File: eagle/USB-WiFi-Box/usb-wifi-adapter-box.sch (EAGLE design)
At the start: 12 parts

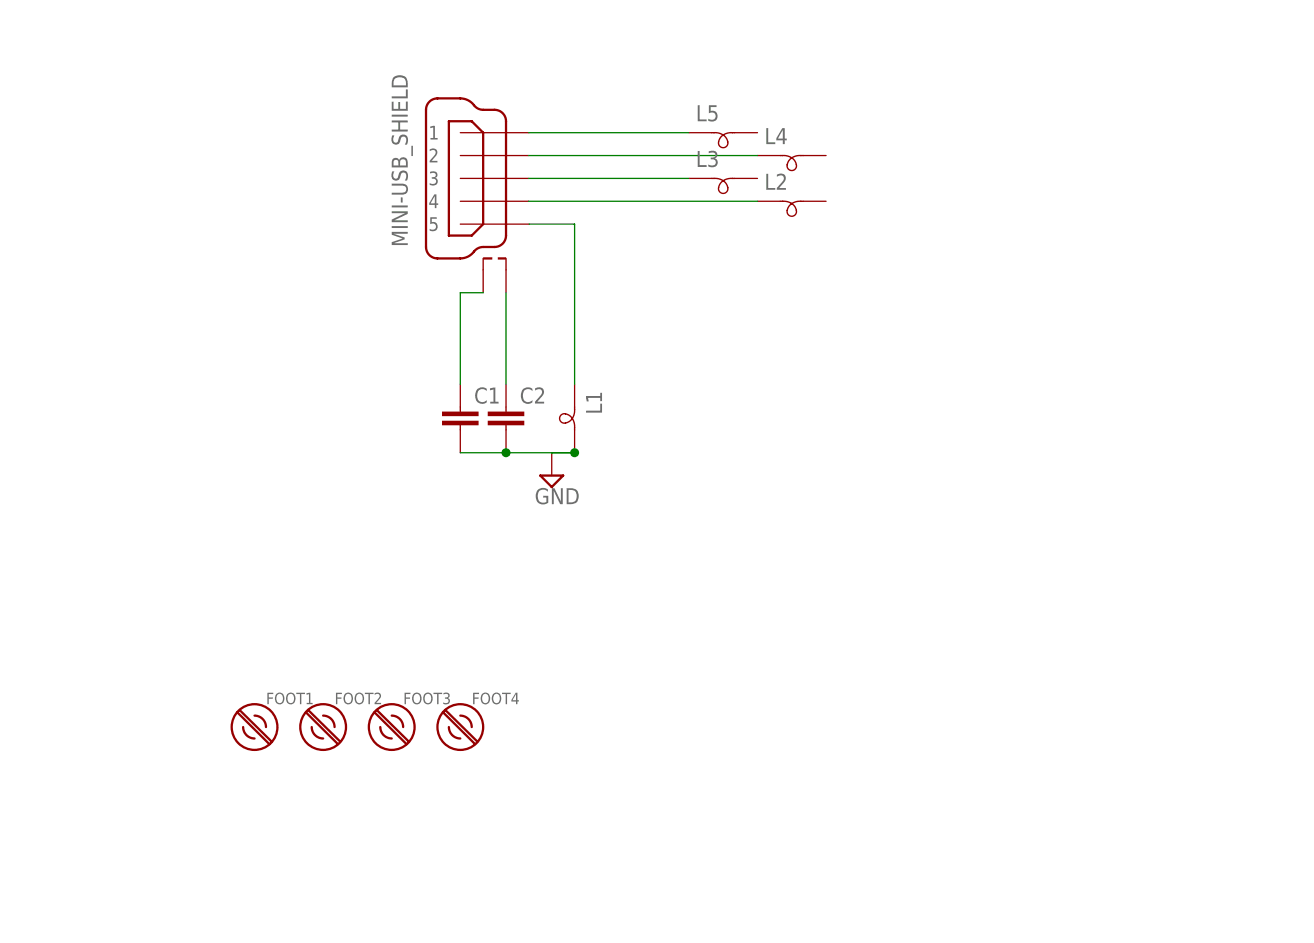
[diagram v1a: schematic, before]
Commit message: Measured USB board, finished schematic
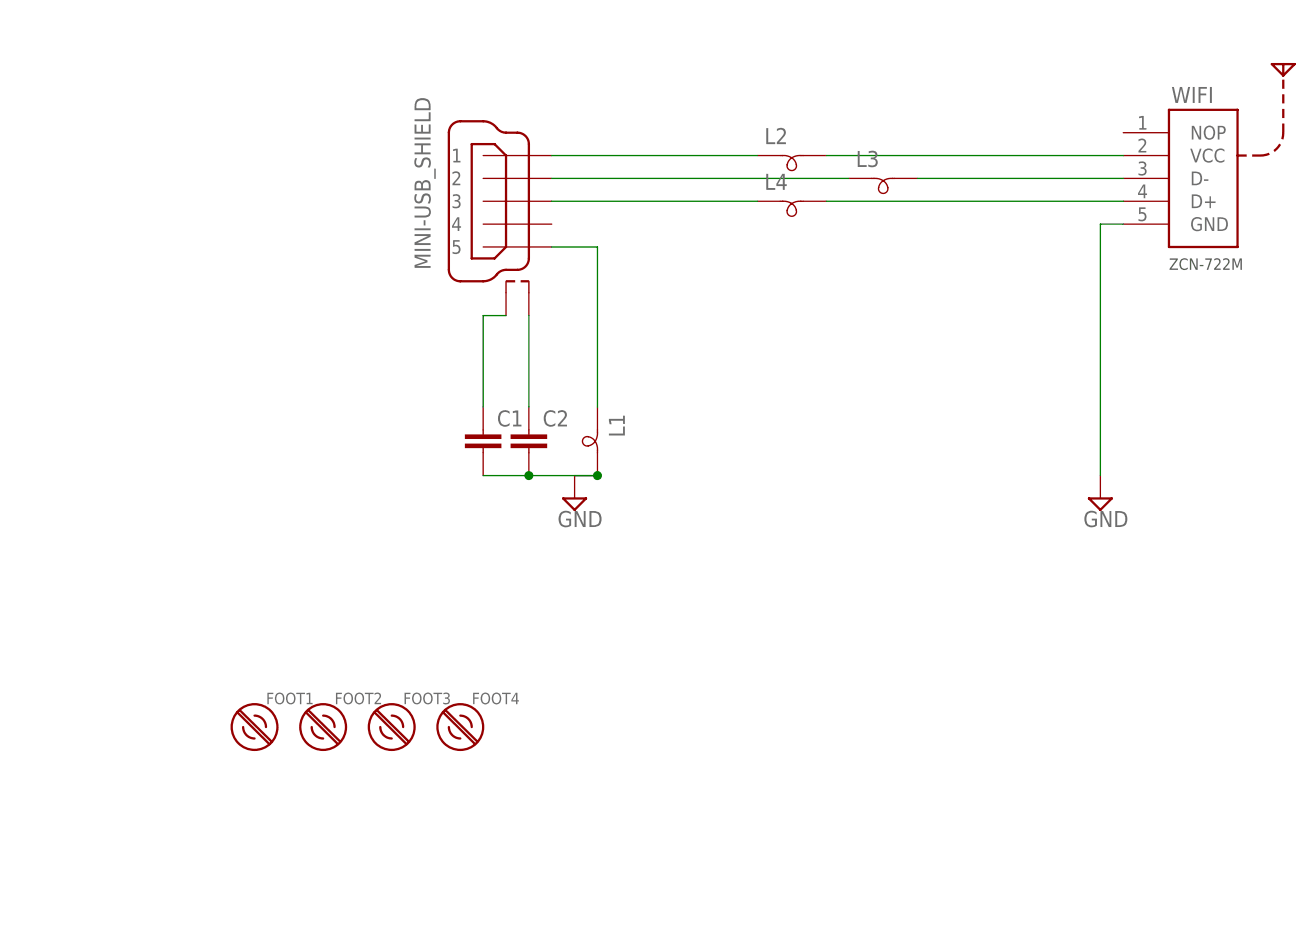
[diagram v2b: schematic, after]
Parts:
- removed L5: (no value), dxwifi:INDUCTOR-BEAD
- added WIFI: ZCN-722M, dxwifi:ZCN-722M
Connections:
- removed net N$2: CONN1G41.4, L2.1
- new net N$10: L4.2, WIFI.D+
- new net N$8: L2.2, WIFI.VCC
- new net N$9: L3.2, WIFI.D-
- net GND: now also WIFI.GND
- net N$3: now also L4.1; no longer L3.1
- net N$4: now also L3.1; no longer L4.1
- net N$5: now also L2.1; no longer L5.1
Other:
- moved on the sheet: C1, C2, L1, L2, L3, L4
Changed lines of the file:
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@@
 <part name="CONN1" library="dxwifi" deviceset="MINI-USB_SHIELD" device=""/>
 <part name="L1" library="dxwifi" deviceset="INDUCTOR-BEAD" device=""/>
+<part name="L4" library="dxwifi" deviceset="INDUCTOR-BEAD" device=""/>
+<part name="L3" library="dxwifi" deviceset="INDUCTOR-BEAD" device=""/>
 <part name="L2" library="dxwifi" deviceset="INDUCTOR-BEAD" device=""/>
-<part name="L3" library="dxwifi" deviceset="INDUCTOR-BEAD" device=""/>
-<part name="L4" library="dxwifi" deviceset="INDUCTOR-BEAD" device=""/>
-<part name="L5" library="dxwifi" deviceset="INDUCTOR-BEAD" device=""/>
 <part name="C1" library="rcl" deviceset="C-EU" device="C0805"/>
 <part name="C2" library="rcl" deviceset="C-EU" device="C0805"/>
@@
 <part name="FOOT4" library="mount-2" deviceset="_4-BARE_MOUNTING_HOLE" device="/.400"/>
 <part name="FRAME1" library="frames" deviceset="A5L-LOC" device=""/>
+<part name="WIFI" library="dxwifi" deviceset="ZCN-722M" device=""/>
+<part name="SUPPLY2" library="supply2" deviceset="GND" device=""/>
 </parts>
 <sheets>
@@
 </plain>
 <instances>
-<instance part="CONN1" gate="G41" x="50.8" y="91.44" smashed="yes" rot="MR0">
-<attribute name="VALUE" x="40.64" y="83.82" size="1.778" layer="96" font="vector" rot="MR90"/>
+<instance part="CONN1" gate="G41" x="53.34" y="88.9" smashed="yes" rot="MR0">
+<attribute name="VALUE" x="43.18" y="81.28" size="1.778" layer="96" font="vector" rot="MR90"/>
 </instance>
-<instance part="L1" gate="G$1" x="60.96" y="63.5" rot="R270"/>
-<instance part="L2" gate="G$1" x="86.36" y="88.9"/>
-<instance part="L3" gate="G$1" x="78.74" y="91.44"/>
-<instance part="L4" gate="G$1" x="86.36" y="93.98"/>
-<instance part="L5" gate="G$1" x="78.74" y="96.52"/>
-<instance part="C1" gate="G$1" x="48.26" y="66.04"/>
-<instance part="C2" gate="G$1" x="53.34" y="66.04"/>
-<instance part="SUPPLY1" gate="GND" x="58.42" y="58.42"/>
-<instance part="CONN1" gate="S" x="53.34" y="81.28" smashed="yes"/>
+<instance part="L1" gate="G$1" x="63.5" y="60.96" rot="R270"/>
+<instance part="L4" gate="G$1" x="86.36" y="88.9"/>
+<instance part="L3" gate="G$1" x="96.52" y="91.44"/>
+<instance part="L2" gate="G$1" x="86.36" y="93.98"/>
+<instance part="C1" gate="G$1" x="50.8" y="63.5"/>
+<instance part="C2" gate="G$1" x="55.88" y="63.5"/>
+<instance part="SUPPLY1" gate="GND" x="60.96" y="55.88"/>
+<instance part="CONN1" gate="S" x="55.88" y="78.74" smashed="yes"/>
 <instance part="FOOT1" gate="MT" x="25.4" y="30.48" smashed="yes">
 <attribute name="NAME" x="26.67" y="33.02" size="1.27" layer="95"/>
@@
 </instance>
 <instance part="FRAME1" gate="G$1" x="0" y="0"/>
+<instance part="WIFI" gate="G$1" x="129.54" y="91.44" smashed="yes">
+<attribute name="NAME" x="127.254" y="99.822" size="1.778" layer="95" font="vector"/>
+</instance>
+<instance part="SUPPLY2" gate="GND" x="119.38" y="55.88"/>
 </instances>
 <busses>
 </busses>
 <nets>
-<net name="N$2" class="0">
-<segment>
-<pinref part="L2" gate="G$1" pin="1"/>
-<pinref part="CONN1" gate="G41" pin="4"/>
-<wire x1="55.88" y1="88.9" x2="81.28" y2="88.9" width="0.1524" layer="91"/>
-</segment>
-</net>
 <net name="N$3" class="0">
 <segment>
 <pinref part="CONN1" gate="G41" pin="3"/>
-<pinref part="L3" gate="G$1" pin="1"/>
-<wire x1="55.88" y1="91.44" x2="73.66" y2="91.44" width="0.1524" layer="91"/>
+<pinref part="L4" gate="G$1" pin="1"/>
+<wire x1="58.42" y1="88.9" x2="81.28" y2="88.9" width="0.1524" layer="91"/>
 </segment>
 </net>
@@
 <segment>
 <pinref part="CONN1" gate="G41" pin="2"/>
-<pinref part="L4" gate="G$1" pin="1"/>
-<wire x1="55.88" y1="93.98" x2="81.28" y2="93.98" width="0.1524" layer="91"/>
+<pinref part="L3" gate="G$1" pin="1"/>
+<wire x1="58.42" y1="91.44" x2="91.44" y2="91.44" width="0.1524" layer="91"/>
 </segment>
 </net>
@@
 <segment>
 <pinref part="CONN1" gate="G41" pin="1"/>
-<pinref part="L5" gate="G$1" pin="1"/>
-<wire x1="55.88" y1="96.52" x2="73.66" y2="96.52" width="0.1524" layer="91"/>
+<pinref part="L2" gate="G$1" pin="1"/>
+<wire x1="58.42" y1="93.98" x2="81.28" y2="93.98" width="0.1524" layer="91"/>
 </segment>
 </net>
@@
 <pinref part="C1" gate="G$1" pin="2"/>
 <pinref part="C2" gate="G$1" pin="2"/>
-<wire x1="48.26" y1="60.96" x2="53.34" y2="60.96" width="0.1524" layer="91"/>
+<wire x1="50.8" y1="58.42" x2="55.88" y2="58.42" width="0.1524" layer="91"/>
 <pinref part="L1" gate="G$1" pin="2"/>
-<wire x1="53.34" y1="60.96" x2="60.96" y2="60.96" width="0.1524" layer="91"/>
-<junction x="53.34" y="60.96"/>
+<wire x1="55.88" y1="58.42" x2="63.5" y2="58.42" width="0.1524" layer="91"/>
+<junction x="55.88" y="58.42"/>
 <pinref part="SUPPLY1" gate="GND" pin="GND"/>
-<junction x="60.96" y="60.96"/>
-<wire x1="60.96" y1="60.96" x2="58.42" y2="60.96" width="0.1524" layer="91"/>
+<junction x="63.5" y="58.42"/>
+<wire x1="63.5" y1="58.42" x2="60.96" y2="58.42" width="0.1524" layer="91"/>
+</segment>
+<segment>
+<pinref part="WIFI" gate="G$1" pin="GND"/>
+<pinref part="SUPPLY2" gate="GND" pin="GND"/>
+<wire x1="121.92" y1="86.36" x2="119.38" y2="86.36" width="0.1524" layer="91"/>
+<wire x1="119.38" y1="86.36" x2="119.38" y2="58.42" width="0.1524" layer="91"/>
 </segment>
 </net>
@@
 <pinref part="CONN1" gate="G41" pin="5"/>
 <pinref part="L1" gate="G$1" pin="1"/>
-<wire x1="55.88" y1="86.36" x2="60.96" y2="86.36" width="0.1524" layer="91"/>
-<wire x1="60.96" y1="86.36" x2="60.96" y2="68.58" width="0.1524" layer="91"/>
+<wire x1="58.42" y1="83.82" x2="63.5" y2="83.82" width="0.1524" layer="91"/>
+<wire x1="63.5" y1="83.82" x2="63.5" y2="66.04" width="0.1524" layer="91"/>
 </segment>
 </net>
@@
 <pinref part="CONN1" gate="S" pin="S2"/>
 <pinref part="C2" gate="G$1" pin="1"/>
-<wire x1="53.34" y1="78.74" x2="53.34" y2="68.58" width="0.1524" layer="91"/>
+<wire x1="55.88" y1="76.2" x2="55.88" y2="66.04" width="0.1524" layer="91"/>
 </segment>
 </net>
@@
 <segment>
 <pinref part="CONN1" gate="S" pin="S1"/>
-<wire x1="50.8" y1="78.74" x2="48.26" y2="78.74" width="0.1524" layer="91"/>
+<wire x1="53.34" y1="76.2" x2="50.8" y2="76.2" width="0.1524" layer="91"/>
 <pinref part="C1" gate="G$1" pin="1"/>
-<wire x1="48.26" y1="78.74" x2="48.26" y2="68.58" width="0.1524" layer="91"/>
+<wire x1="50.8" y1="76.2" x2="50.8" y2="66.04" width="0.1524" layer="91"/>
 </segment>
 </net>
+<net name="N$8" class="0">
+<segment>
+<pinref part="L2" gate="G$1" pin="2"/>
+<pinref part="WIFI" gate="G$1" pin="VCC"/>
+<wire x1="88.9" y1="93.98" x2="121.92" y2="93.98" width="0.1524" layer="91"/>
+</segment>
+</net>
+<net name="N$9" class="0">
+<segment>
+<pinref part="L3" gate="G$1" pin="2"/>
+<pinref part="WIFI" gate="G$1" pin="D-"/>
+<wire x1="99.06" y1="91.44" x2="121.92" y2="91.44" width="0.1524" layer="91"/>
+</segment>
+</net>
+<net name="N$10" class="0">
+<segment>
+<pinref part="L4" gate="G$1" pin="2"/>
+<pinref part="WIFI" gate="G$1" pin="D+"/>
+<wire x1="88.9" y1="88.9" x2="121.92" y2="88.9" width="0.1524" layer="91"/>
+</segment>
+</net>

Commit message: board layout v1, using one wire for VCC, fixed slots in USB part
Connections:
- net N$1 renamed SHEILDGND1
- net N$10 renamed D+
- net N$3 renamed D+OUT
- net N$4 renamed D-OUT
- net N$5 renamed VCC_OUT
- net N$6 renamed GNDOUT
- net N$7 renamed SHIELDGND2
- net N$8 renamed VCC
- net N$9 renamed D-
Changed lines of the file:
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@@
 </busses>
 <nets>
-<net name="N$3" class="0">
+<net name="D+OUT" class="0">
 <segment>
 <pinref part="CONN1" gate="G41" pin="3"/>
@@
 </segment>
 </net>
-<net name="N$4" class="0">
+<net name="D-OUT" class="0">
 <segment>
 <pinref part="CONN1" gate="G41" pin="2"/>
@@
 </segment>
 </net>
-<net name="N$5" class="0">
+<net name="VCC_OUT" class="0">
 <segment>
 <pinref part="CONN1" gate="G41" pin="1"/>
@@
 </segment>
 </net>
-<net name="N$6" class="0">
+<net name="GNDOUT" class="0">
 <segment>
 <pinref part="CONN1" gate="G41" pin="5"/>
@@
 </segment>
 </net>
-<net name="N$1" class="0">
+<net name="SHEILDGND1" class="0">
 <segment>
 <pinref part="CONN1" gate="S" pin="S2"/>
@@
 </segment>
 </net>
-<net name="N$7" class="0">
+<net name="SHIELDGND2" class="0">
 <segment>
 <pinref part="CONN1" gate="S" pin="S1"/>
@@
 </segment>
 </net>
-<net name="N$8" class="0">
+<net name="VCC" class="0">
 <segment>
 <pinref part="L2" gate="G$1" pin="2"/>
@@
 </segment>
 </net>
-<net name="N$9" class="0">
+<net name="D-" class="0">
 <segment>
 <pinref part="L3" gate="G$1" pin="2"/>
@@
 </segment>
 </net>
-<net name="N$10" class="0">
+<net name="D+" class="0">
 <segment>
 <pinref part="L4" gate="G$1" pin="2"/>

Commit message: fix routing issues
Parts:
- added TP1: PTR1PAD1-13, testpad:PTR1PAD1-13
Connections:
- new net N$1: TP1.TP, WIFI.NOP
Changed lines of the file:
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@@
 <part name="WIFI" library="dxwifi" deviceset="ZCN-722M" device=""/>
 <part name="SUPPLY2" library="supply2" deviceset="GND" device=""/>
+<part name="TP1" library="testpad" deviceset="PTR1" device="PAD1-13"/>
 </parts>
 <sheets>
@@
 </instance>
 <instance part="SUPPLY2" gate="GND" x="119.38" y="55.88"/>
+<instance part="TP1" gate="G$1" x="119.38" y="99.06" rot="R180"/>
 </instances>
 <busses>
@@
 </segment>
 </net>
+<net name="N$1" class="0">
+<segment>
+<pinref part="TP1" gate="G$1" pin="TP"/>
+<pinref part="WIFI" gate="G$1" pin="NOP"/>
+<wire x1="119.38" y1="96.52" x2="121.92" y2="96.52" width="0.1524" layer="91"/>
+</segment>
+</net>

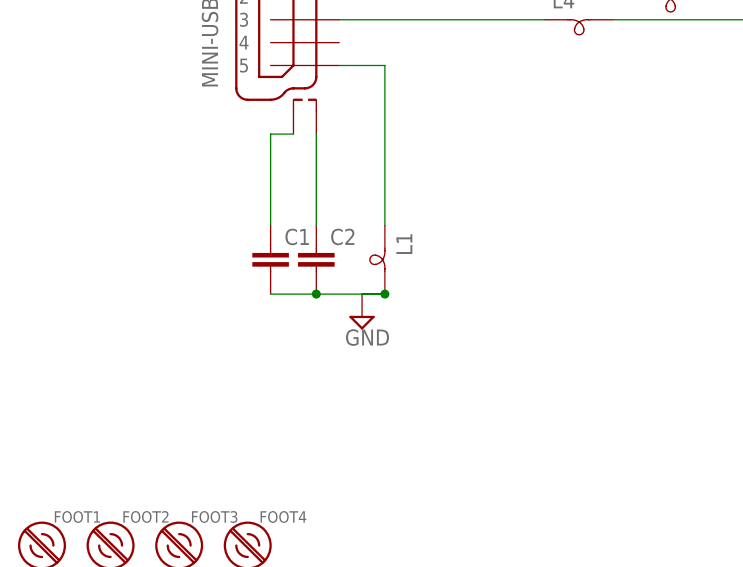
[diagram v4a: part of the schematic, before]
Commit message: minor fixes, values of caps
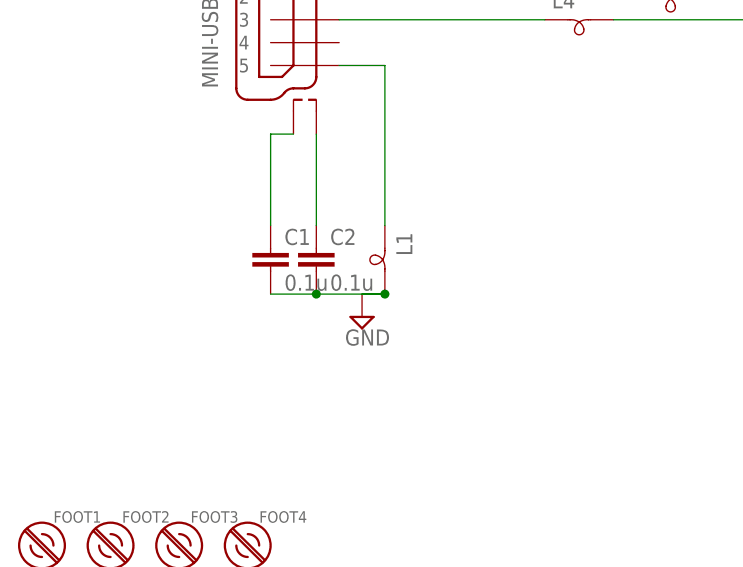
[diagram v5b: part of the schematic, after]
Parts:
- C1, C2: value (none) -> 0.1u
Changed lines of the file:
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@@
 <part name="L3" library="dxwifi" deviceset="INDUCTOR-BEAD" device=""/>
 <part name="L2" library="dxwifi" deviceset="INDUCTOR-BEAD" device=""/>
-<part name="C1" library="rcl" deviceset="C-EU" device="C0805"/>
-<part name="C2" library="rcl" deviceset="C-EU" device="C0805"/>
+<part name="C1" library="rcl" deviceset="C-EU" device="C0805" value="0.1u"/>
+<part name="C2" library="rcl" deviceset="C-EU" device="C0805" value="0.1u"/>
 <part name="SUPPLY1" library="supply2" deviceset="GND" device=""/>
 <part name="FOOT1" library="mount-2" deviceset="_4-BARE_MOUNTING_HOLE" device="/.400"/>
